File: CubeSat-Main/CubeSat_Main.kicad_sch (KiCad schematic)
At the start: 21 parts, among them J1 Conn_01x03_Pin, J2 Conn_01x08_Socket, U1 STM32F411CEU6 - BlackPill, U2 LORA E220-900T22D, U3 BNO055, U4 GPS_NEO6M, U5 LM7805_TO220, U6 LM35-LP

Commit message: Mostly fine tuning the boards, also added capacitor for battery ADC
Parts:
- added C4: 0.1uF, Capacitor_THT:C_Disc_D8.0mm_W2.5mm_P5.00mm, symbol Device:C
- added J3: Conn_01x03_Pin, Connector_PinHeader_2.54mm:PinHeader_1x03_P2.54mm_Vertical, symbol Connector:Conn_01x03_Pin
- C2, C3: footprint Capacitor_THT:C_Disc_D8.0mm_W5.0mm_P7.50mm -> Capacitor_THT:C_Disc_D8.0mm_W2.5mm_P5.00mm
- R6: value 100K -> 10K
- R7: value 47K -> 4.7K
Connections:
- net 5V_LDO: now also J3.3 (Pin_3); no longer U2.6 (VCC), U6.1 (+V_{S})
- net GND: now also C3.1, C4.1; no longer C3.2
- net STM_3.3V: no longer C3.1, U3.1 (VIN)
- net VIN_5V: now also J3.1 (Pin_1)
- net Vbat_ADC: now also C4.2
- net VIN_5V2: now reaches U1.5V2 (5V)
- net VIN_5V2: now also C3.2, U3.1 (VIN)
- new net 5V_E220: J3.2 (Pin_2), U2.6 (VCC), U6.1 (+V_{S})
- no-connect marks 23 -> 22
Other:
- note added: "JUMPER"
- note removed: "SAFETY JUMPER"
- moved on the sheet: C1, C2, R7, U1, U5

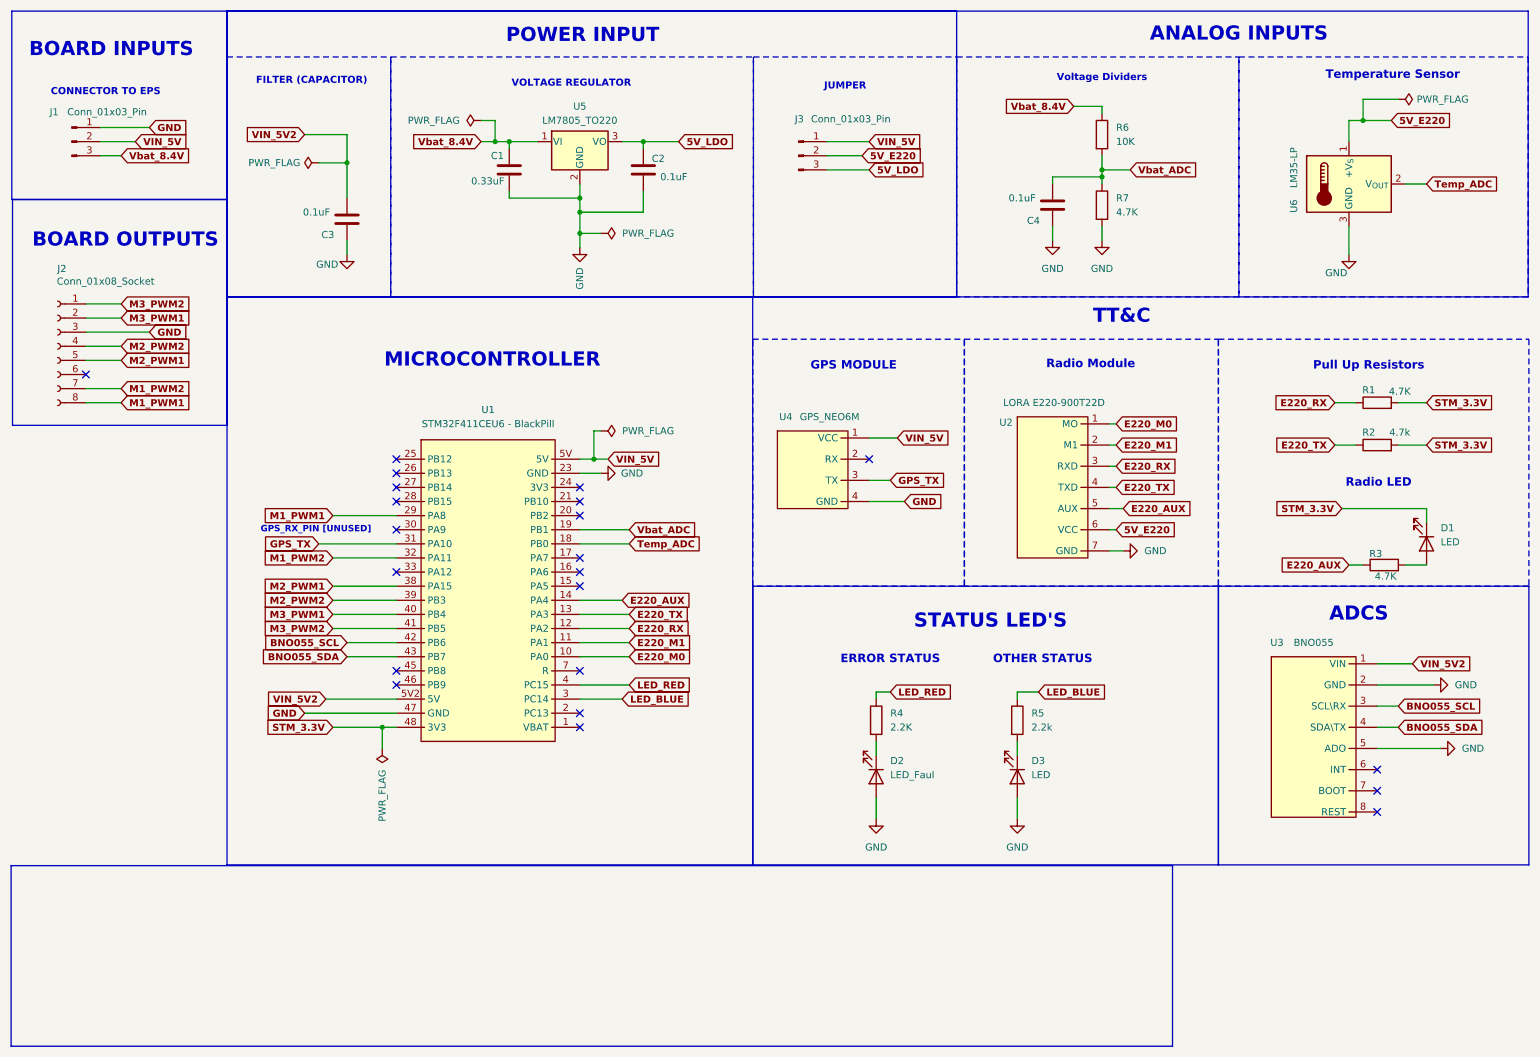
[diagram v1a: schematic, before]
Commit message: Changing the size of all traces to fit the 1 mm requirement of the draft PCB
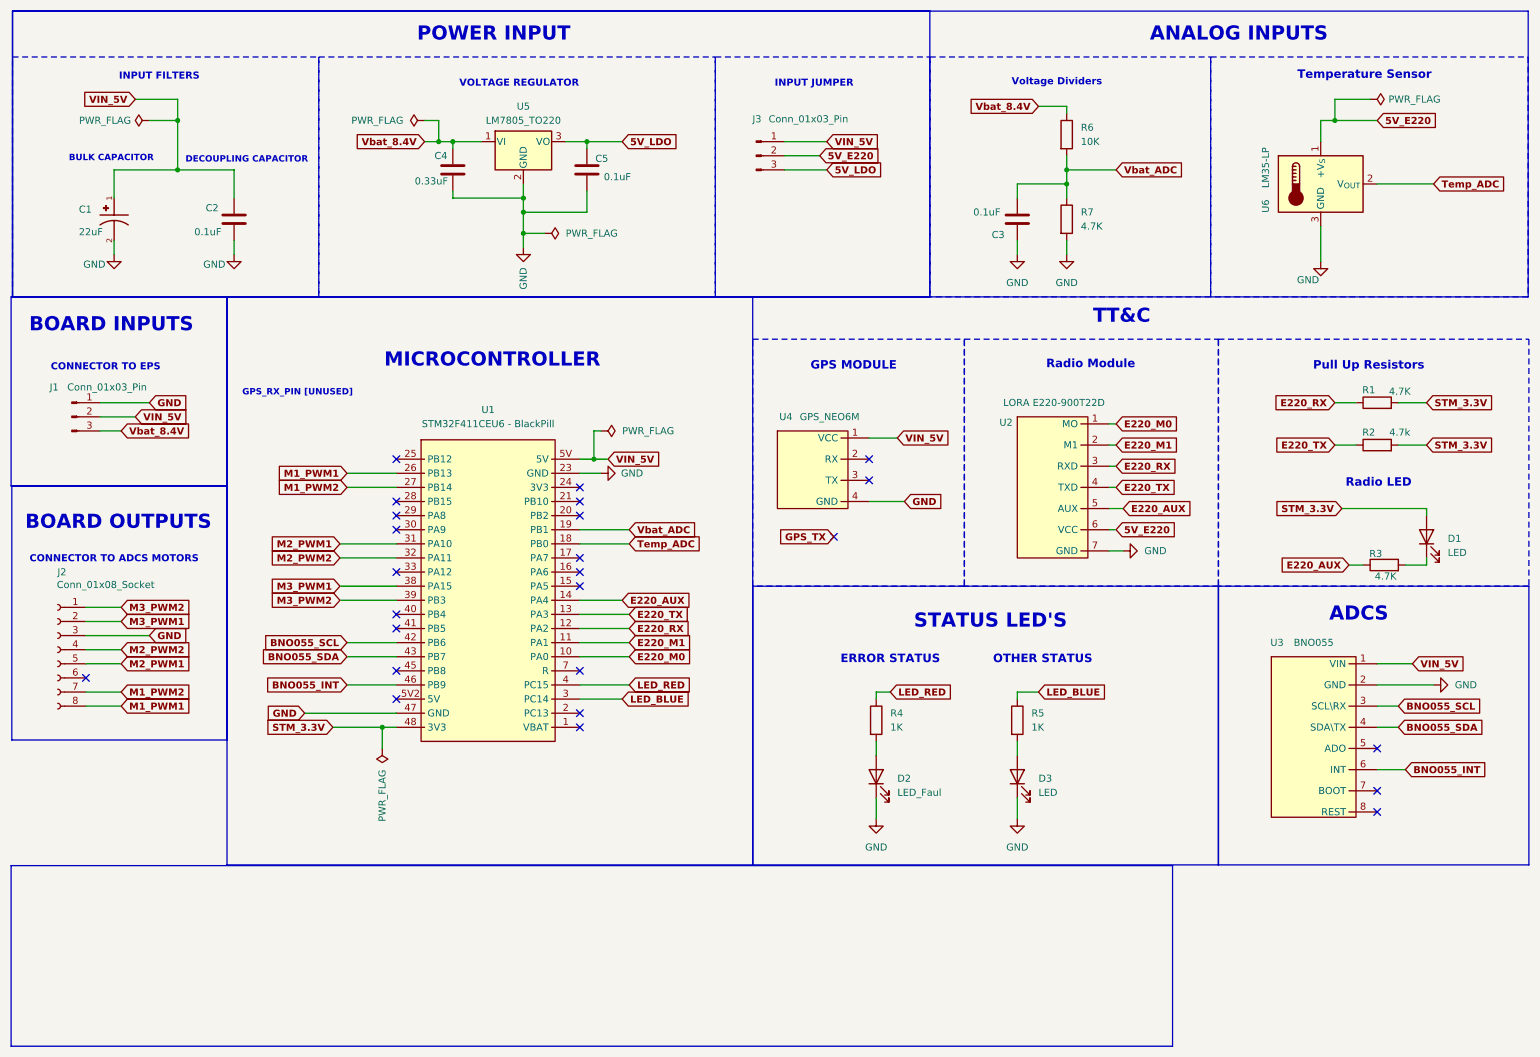
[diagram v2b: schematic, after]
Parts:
- added C1: 22uF, Cubesat_Modules:Cap_Electrolytic, symbol Cubesat_Modules:Cap_Electrolytic
- C2: renamed from C3; footprint Capacitor_THT:C_Disc_D8.0mm_W2.5mm_P5.00mm -> Capacitor_THT:C_Disc_D8.0mm_W5.0mm_P5.00mm
- C3: renamed from C4; footprint Capacitor_THT:C_Disc_D8.0mm_W2.5mm_P5.00mm -> Capacitor_THT:C_Disc_D8.0mm_W5.0mm_P5.00mm
- D1, D2, D3: footprint LED_THT:LED_D3.0mm_Horizontal_O1.27mm_Z2.0mm -> LED_THT:LED_D3.0mm
- R4: value 2.2K -> 1K
- R5: value 2.2k -> 1K
- U6: footprint Package_TO_SOT_THT:TO-92_Inline -> Cubesat_Modules:LM35DZ
- renumbered C1 to C4, C2 to C5
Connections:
- net GND: now also D2.1 (K), D3.1 (K), C1.2; no longer D2.2 (A), D3.2 (A), U3.5 (ADO)
- net GPS_TX: no longer U1.31 (PA10), U4.3 (TX)
- net M1_PWM1: now also U1.26 (PB13); no longer U1.29 (PA8)
- net M1_PWM2: now also U1.27 (PB14); no longer U1.32 (PA11)
- net M2_PWM1: now also U1.31 (PA10); no longer U1.38 (PA15)
- net M2_PWM2: now also U1.32 (PA11); no longer U1.39 (PB3)
- net M3_PWM1: now also U1.38 (PA15); no longer U1.40 (PB4)
- net M3_PWM2: now also U1.39 (PB3); no longer U1.41 (PB5)
- net STM_3.3V: now also D1.2 (A); no longer D1.1 (K)
- net VIN_5V: now also C2.2, U3.1 (VIN), C1.1
- net at R5.2: now also D3.2 (A); no longer D3.1 (K)
- net BNO055_INT: now reaches U3.6 (INT)
- net BNO055_INT: now also U1.46 (PB9)
- net at R3.2: now also D1.1 (K); no longer D1.2 (A)
- net at R4.2: now also D2.2 (A); no longer D2.1 (K)
- removed net VIN_5V2: C2.2, U1.5V2 (5V), U3.1 (VIN)
- no-connect marks 22 -> 25
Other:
- note added: "BULK CAPACITOR"
- note added: "CONNECTOR TO ADCS MOTORS"
- note added: "DECOUPLING CAPACITOR"
- note added: "INPUT FILTERS"
- note added: "INPUT JUMPER"
- note removed: "FILTER (CAPACITOR)"
- note removed: "JUMPER"
- moved on the sheet: C2, C3, C4, C5, D1, D2, D3, J1, J2, J3, R6, R7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

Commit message: final changes
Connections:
- net M3_PWM1: now also U1.40 (PB4); no longer U1.38 (PA15)
- net M3_PWM2: now also U1.41 (PB5); no longer U1.39 (PB3)
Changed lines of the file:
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@@
-	)
-	(no_connect
-		(at 81.28 120.65)
 	)
 	(no_connect
@@
 	)
 	(no_connect
-		(at 81.28 123.19)
-	)
-	(no_connect
 		(at 114.3 140.97)
 	)
@@
 	)
 	(no_connect
+		(at 81.28 118.11)
+	)
+	(no_connect
 		(at 257.81 152.4)
 	)
@@
 	)
 	(no_connect
+		(at 81.28 115.57)
+	)
+	(no_connect
 		(at 160.02 106.68)
 	)
@@
 	(wire
 		(pts
+			(xy 71.12 120.65) (xy 81.28 120.65)
+		)
+		(stroke
+			(width 0)
+			(type default)
+		)
+	)
+	(wire
+		(pts
 			(xy 71.12 107.95) (xy 81.28 107.95)
 		)
@@
 	(wire
 		(pts
-			(xy 71.12 115.57) (xy 81.28 115.57)
-		)
-		(stroke
-			(width 0)
-			(type default)
-		)
-	)
-	(wire
-		(pts
 			(xy 201.93 40.64) (xy 201.93 43.18)
 		)
@@
 	(wire
 		(pts
+			(xy 71.12 123.19) (xy 81.28 123.19)
+		)
+		(stroke
+			(width 0)
+			(type default)
+		)
+	)
+	(wire
+		(pts
 			(xy 72.39 95.25) (xy 81.28 95.25)
 		)
@@
 	(wire
 		(pts
-			(xy 71.12 118.11) (xy 81.28 118.11)
-		)
-		(stroke
-			(width 0)
-			(type default)
-		)
-	)
-	(wire
-		(pts
 			(xy 257.81 133.35) (xy 267.97 133.35)
 		)
@@
 	(global_label "M3_PWM2"
 		(shape input)
-		(at 71.12 118.11 180)
+		(at 71.12 123.19 180)
 		(fields_autoplaced yes)
 		(effects
@@
 		)
 		(property "Intersheetrefs" "${INTERSHEET_REFS}"
-			(at 58.648 118.11 0)
+			(at 58.648 123.19 0)
 			(effects
 				(font
@@
 	(global_label "M3_PWM1"
 		(shape input)
-		(at 71.12 115.57 180)
+		(at 71.12 120.65 180)
 		(fields_autoplaced yes)
 		(effects
@@
 		)
 		(property "Intersheetrefs" "${INTERSHEET_REFS}"
-			(at 58.648 115.57 0)
-			(effects
-				(font
+			(at 58.648 120.65 0)
+			(effects
+				(font

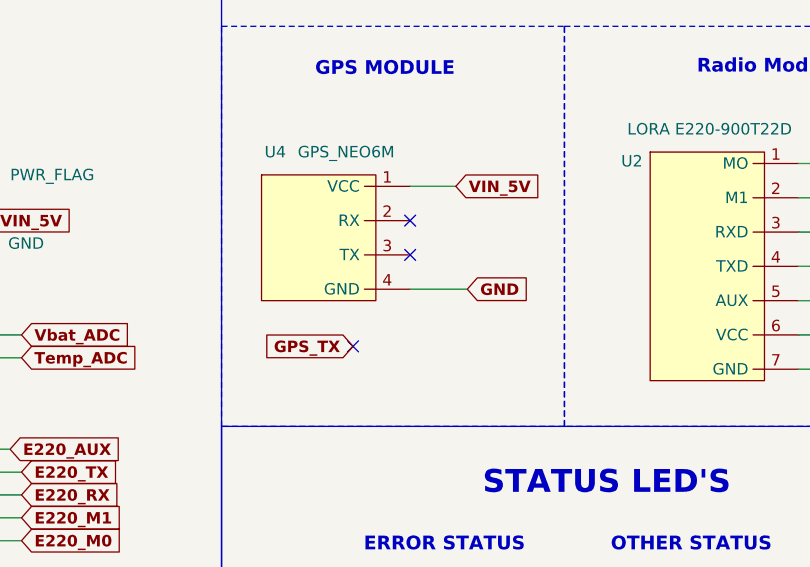
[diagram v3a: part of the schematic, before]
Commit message: add new drill format
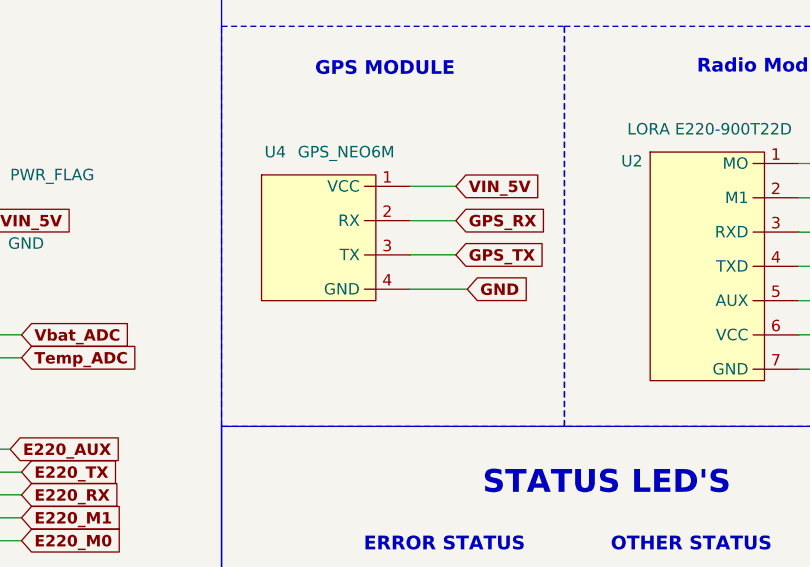
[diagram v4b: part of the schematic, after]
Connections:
- net GPS_TX: now also U4.3 (TX)
- net GPS_RX: now reaches U4.2 (RX)
- no-connect marks 25 -> 22

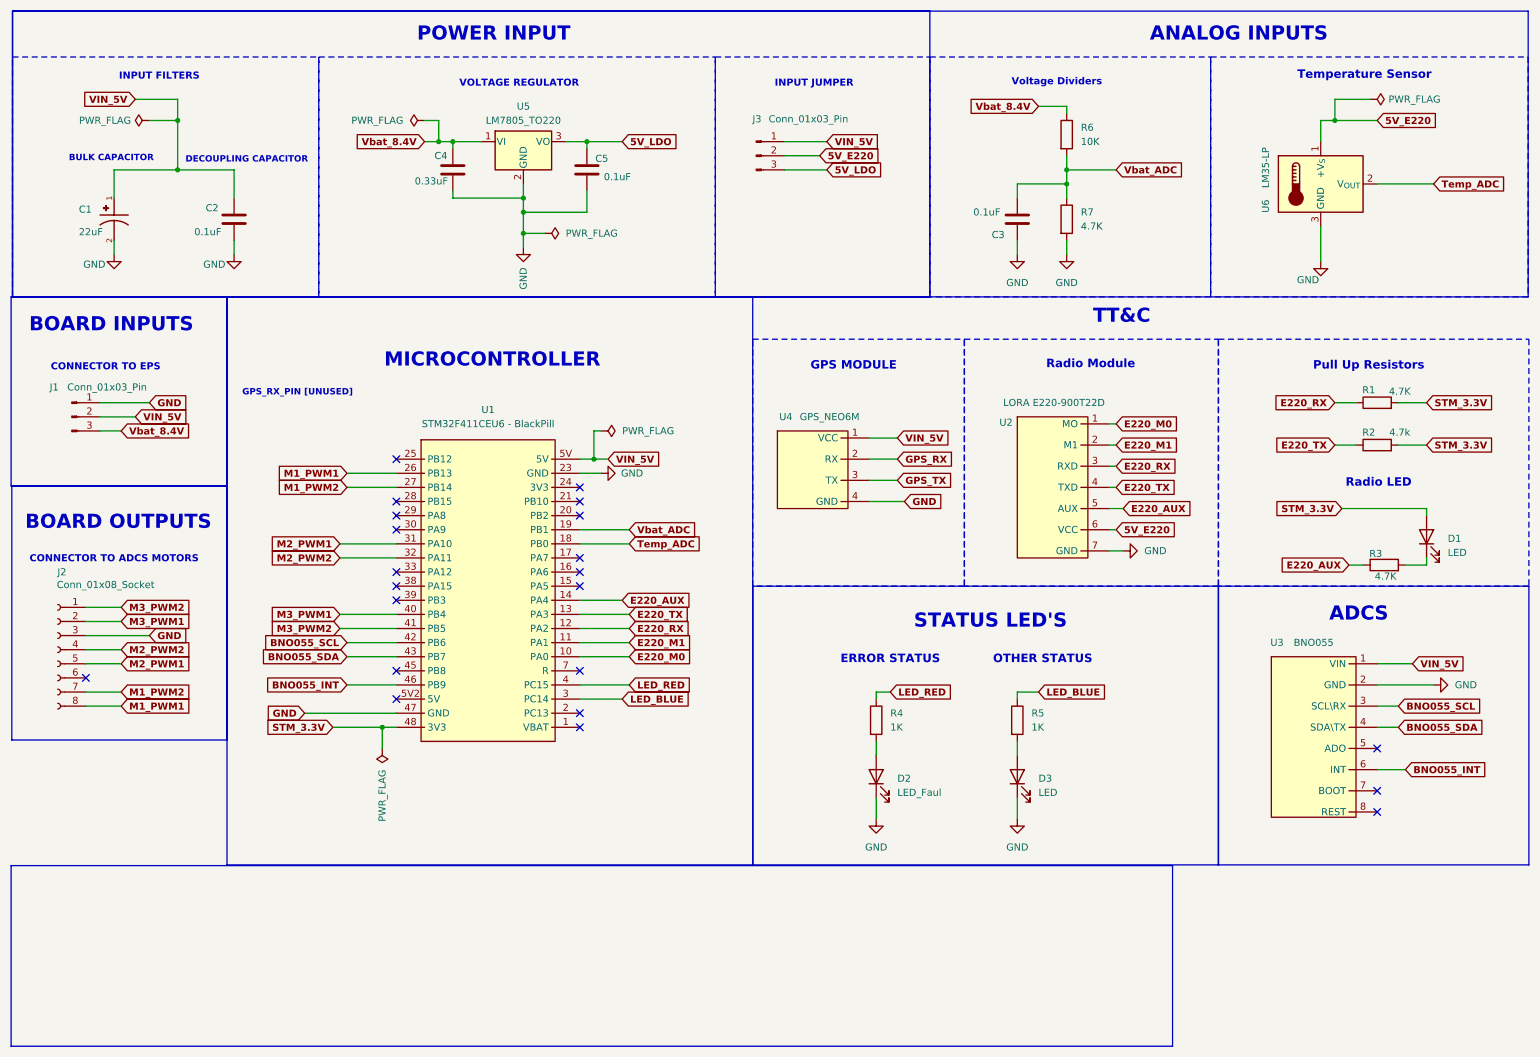
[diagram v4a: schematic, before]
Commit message: final changes in ALL 3 pcbs: mounting wholes config, and a few connector changes
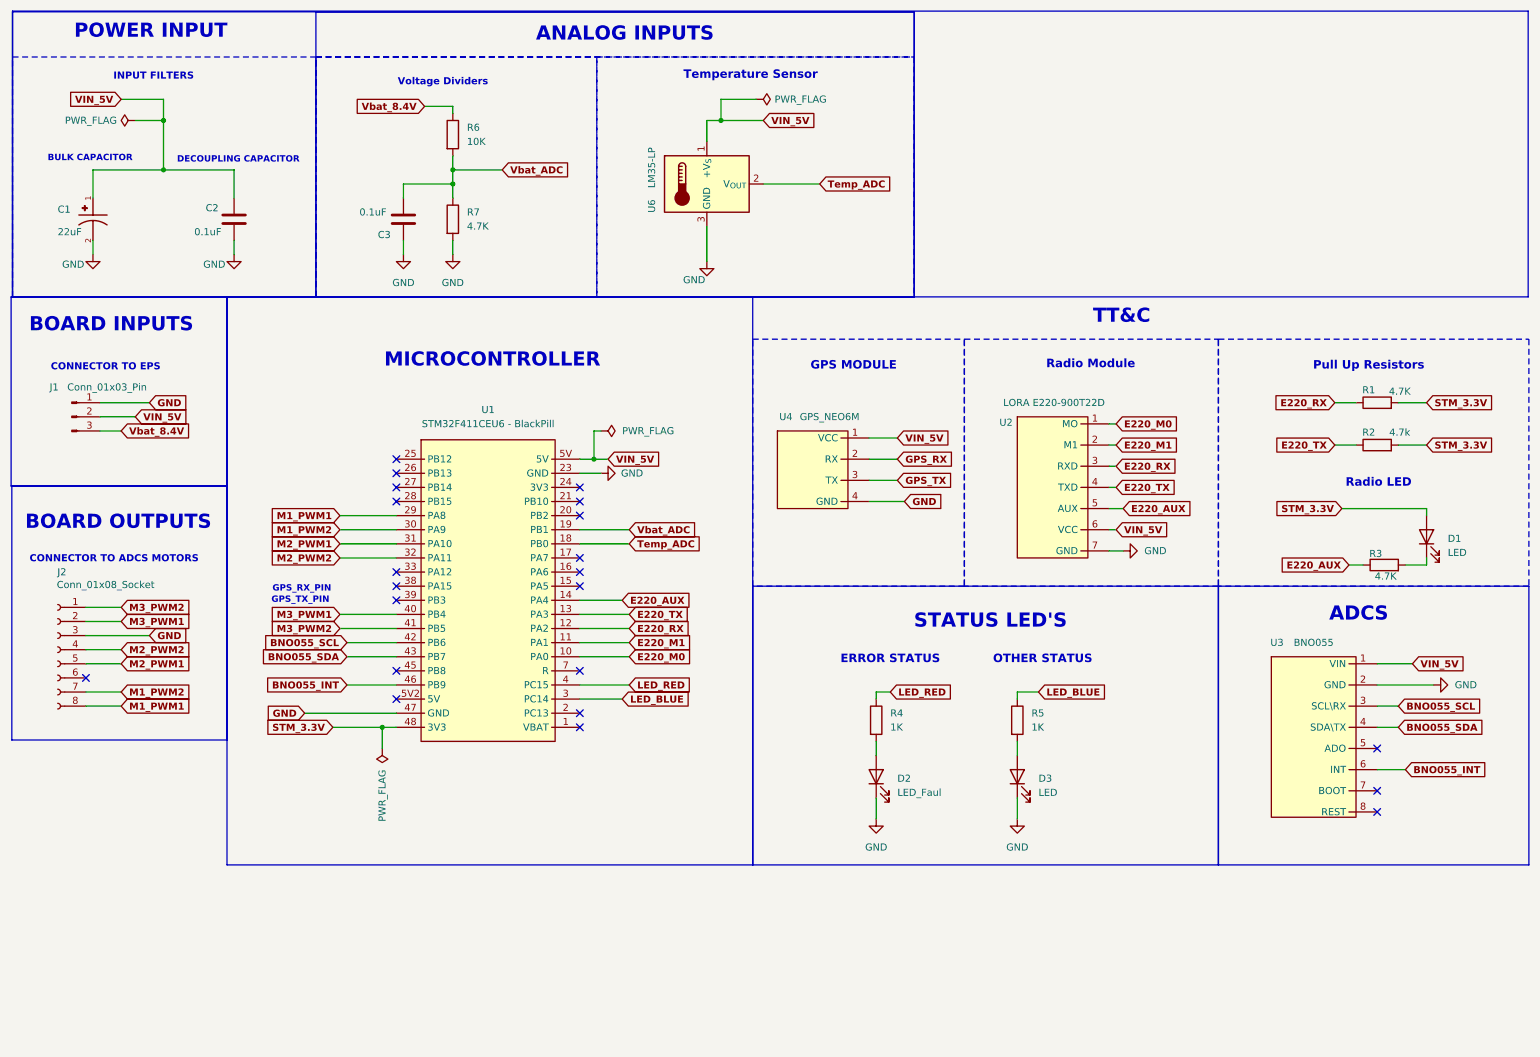
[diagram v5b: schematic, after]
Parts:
- removed C4: 0.33uF, Capacitor_THT:C_Disc_D8.0mm_W5.0mm_P7.50mm, symbol Device:C
- removed C5: 0.1uF, Capacitor_THT:C_Disc_D8.0mm_W2.5mm_P5.00mm, symbol Device:C
- removed J3: Conn_01x03_Pin, Connector_PinHeader_2.54mm:PinHeader_1x03_P2.54mm_Vertical, symbol Connector:Conn_01x03_Pin
- removed U5: LM7805_TO220, Package_TO_SOT_THT:TO-220-3_Vertical, symbol Regulator_Linear:LM7805_TO220
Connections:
- net 5V_E220 is gone; now on net VIN_5V: U2.6 (VCC), U6.1 (+V_{S})
- net M1_PWM1: now also U1.29 (PA8); no longer U1.26 (PB13)
- net M1_PWM2: now also U1.30 (PA9); no longer U1.27 (PB14)
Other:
- note added: "GPS_RX_PIN"
- note added: "GPS_TX_PIN"
- note removed: "GPS_RX_PIN [UNUSED]"
- note removed: "INPUT JUMPER"
- note removed: "VOLTAGE REGULATOR"
- moved on the sheet: C1, C3, R6, R7, U6
